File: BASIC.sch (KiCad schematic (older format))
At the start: 2 parts, among them U4 BASIC_ROM

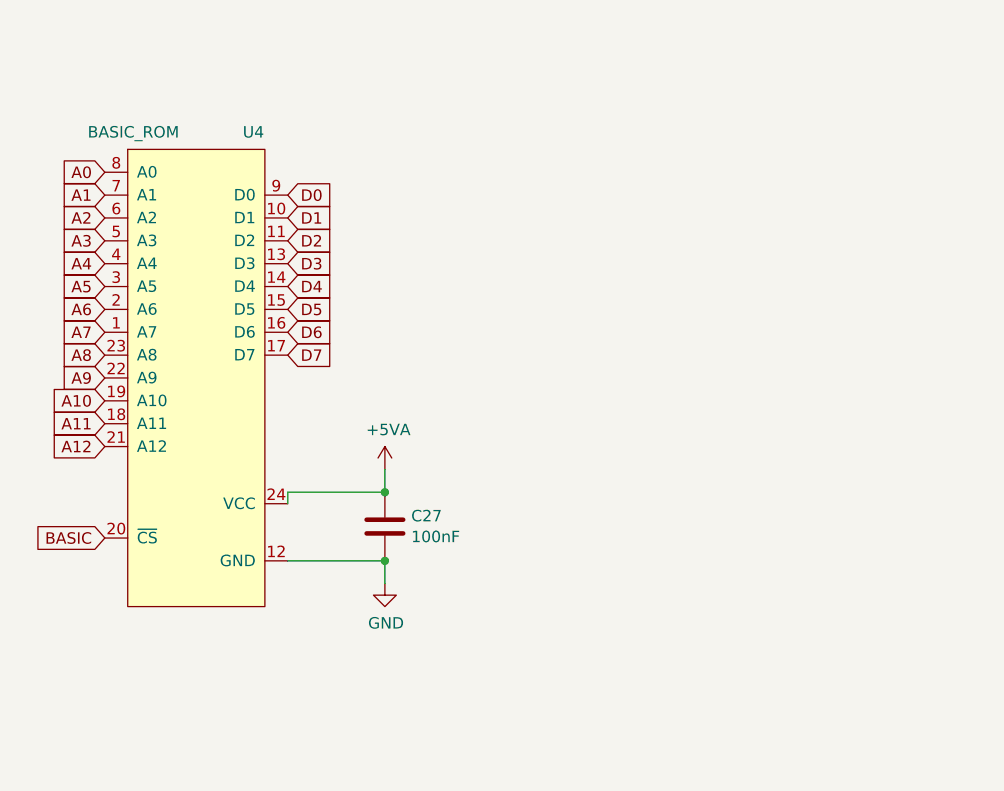
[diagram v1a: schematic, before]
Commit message: OSS and Basic in PLCC
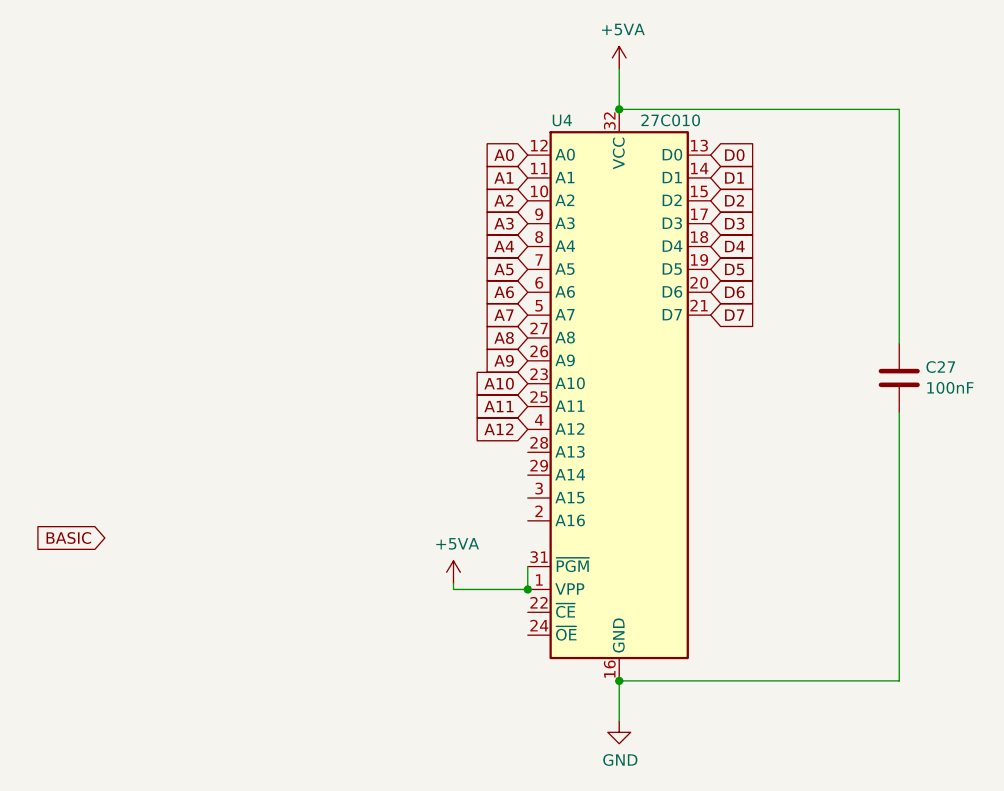
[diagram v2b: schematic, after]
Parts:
- removed U4: BASIC_ROM, Package_DIP:DIP-24_W15.24mm_Socket, symbol Atari:BASIC_ROM
- added U4: 27C010, Atari:PLCC-32_THT-Socket, symbol Memory_EPROM:27C010
- C27: footprint Atari:C_Axial_L5.1mm_D2.5mm_P12.50mm_Horizontal -> Capacitor_SMD:C_1206_3216Metric_Pad1.42x1.75mm_HandSolder
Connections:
- net +5VA: now also U4.1 (VPP), U4.31 (~PGM), U4.32 (VCC)
- net A0: now also U4.12 (A0)
- net A1: now also U4.11 (A1)
- net A10: now also U4.23 (A10)
- net A11: now also U4.25 (A11)
- net A12: now also U4.4 (A12)
- net A2: now also U4.10 (A2)
- net A3: now also U4.9 (A3)
- net A4: now also U4.8 (A4)
- net A5: now also U4.7 (A5)
- net A6: now also U4.6 (A6)
- net A7: now also U4.5 (A7)
- net A8: now also U4.27 (A8)
- net A9: now also U4.26 (A9)
- net D0: now also U4.13 (D0)
- net D1: now also U4.14 (D1)
- net D2: now also U4.15 (D2)
- net D3: now also U4.17 (D3)
- net D4: now also U4.18 (D4)
- net D5: now also U4.19 (D5)
- net D6: now also U4.20 (D6)
- net D7: now also U4.21 (D7)
- net GND: now also U4.16 (GND)
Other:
- moved on the sheet: C27
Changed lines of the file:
@@
 Comment4 ""
 $EndDescr
-Text GLabel 5675 2850 2    50   Input ~ 0
+Text GLabel 7525 2675 2    50   Input ~ 0
 D0
-Text GLabel 5675 2950 2    50   Input ~ 0
+Text GLabel 7525 2775 2    50   Input ~ 0
 D1
-Text GLabel 5675 3050 2    50   Input ~ 0
+Text GLabel 7525 2875 2    50   Input ~ 0
 D2
-Text GLabel 5675 3150 2    50   Input ~ 0
+Text GLabel 7525 2975 2    50   Input ~ 0
 D3
-Text GLabel 5675 3250 2    50   Input ~ 0
+Text GLabel 7525 3075 2    50   Input ~ 0
 D4
-Text GLabel 5675 3350 2    50   Input ~ 0
+Text GLabel 7525 3175 2    50   Input ~ 0
 D5
-Text GLabel 5675 3450 2    50   Input ~ 0
+Text GLabel 7525 3275 2    50   Input ~ 0
 D6
-Text GLabel 5675 3550 2    50   Input ~ 0
+Text GLabel 7525 3375 2    50   Input ~ 0
 D7
-Text GLabel 4875 2750 0    50   Input ~ 0
+Text GLabel 6725 2675 0    50   Input ~ 0
 A0
-Text GLabel 4875 2850 0    50   Input ~ 0
+Text GLabel 6725 2775 0    50   Input ~ 0
 A1
-Text GLabel 4875 2950 0    50   Input ~ 0
+Text GLabel 6725 2875 0    50   Input ~ 0
 A2
-Text GLabel 4875 3050 0    50   Input ~ 0
+Text GLabel 6725 2975 0    50   Input ~ 0
 A3
-Text GLabel 4875 3150 0    50   Input ~ 0
+Text GLabel 6725 3075 0    50   Input ~ 0
 A4
-Text GLabel 4875 3250 0    50   Input ~ 0
+Text GLabel 6725 3175 0    50   Input ~ 0
 A5
-Text GLabel 4875 3350 0    50   Input ~ 0
+Text GLabel 6725 3275 0    50   Input ~ 0
 A6
-Text GLabel 4875 3450 0    50   Input ~ 0
+Text GLabel 6725 3375 0    50   Input ~ 0
 A7
-Text GLabel 4875 3550 0    50   Input ~ 0
+Text GLabel 6725 3475 0    50   Input ~ 0
 A8
-Text GLabel 4875 3650 0    50   Input ~ 0
+Text GLabel 6725 3575 0    50   Input ~ 0
 A9
-Text GLabel 4875 3750 0    50   Input ~ 0
+Text GLabel 6725 3675 0    50   Input ~ 0
 A10
-Text GLabel 4875 3850 0    50   Input ~ 0
+Text GLabel 6725 3775 0    50   Input ~ 0
 A11
-Text GLabel 4875 3950 0    50   Input ~ 0
+Text GLabel 6725 3875 0    50   Input ~ 0
 A12
 Text GLabel 4875 4350 0    50   Input ~ 0
@@
 L Device:C C27
 U 1 1 6020CFCE
-P 6100 4300
-F 0 "C27" H 6215 4346 50  0000 L CNN
-F 1 "100nF" H 6215 4255 50  0000 L CNN
-F 2 "Atari:C_Axial_L5.1mm_D2.5mm_P12.50mm_Horizontal" H 6138 4150 50  0001 C CNN
-F 3 "~" H 6100 4300 50  0001 C CNN
-	1    6100 4300
+P 8350 3650
+F 0 "C27" H 8465 3696 50  0000 L CNN
+F 1 "100nF" H 8465 3605 50  0000 L CNN
+F 2 "Capacitor_SMD:C_1206_3216Metric_Pad1.42x1.75mm_HandSolder" H 8388 3500 50  0001 C CNN
+F 3 "~" H 8350 3650 50  0001 C CNN
+	1    8350 3650
 	1    0    0    -1
 $EndComp
@@
 L power:+5VA #PWR0145
 U 1 1 6020DDBE
-P 6100 4050
-F 0 "#PWR0145" H 6100 3900 50  0001 C CNN
-F 1 "+5VA" H 6115 4223 50  0000 C CNN
-F 2 "" H 6100 4050 50  0001 C CNN
-F 3 "" H 6100 4050 50  0001 C CNN
-	1    6100 4050
+P 7125 2300
+F 0 "#PWR0145" H 7125 2150 50  0001 C CNN
+F 1 "+5VA" H 7140 2473 50  0000 C CNN
+F 2 "" H 7125 2300 50  0001 C CNN
+F 3 "" H 7125 2300 50  0001 C CNN
+	1    7125 2300
 	1    0    0    -1
 $EndComp
@@
 L power:GND #PWR0146
 U 1 1 6020E6E5
-P 6100 4550
-F 0 "#PWR0146" H 6100 4300 50  0001 C CNN
-F 1 "GND" H 6105 4377 50  0000 C CNN
-F 2 "" H 6100 4550 50  0001 C CNN
-F 3 "" H 6100 4550 50  0001 C CNN
-	1    6100 4550
+P 7125 5150
+F 0 "#PWR0146" H 7125 4900 50  0001 C CNN
+F 1 "GND" H 7130 4977 50  0000 C CNN
+F 2 "" H 7125 5150 50  0001 C CNN
+F 3 "" H 7125 5150 50  0001 C CNN
+	1    7125 5150
 	1    0    0    -1
 $EndComp
 $Comp
-L Atari:BASIC_ROM U4
-U 1 1 60211097
-P 5275 3650
-F 0 "U4" H 5525 4725 50  0000 C CNN
-F 1 "BASIC_ROM" H 5000 4725 50  0000 C CNN
-F 2 "Package_DIP:DIP-24_W15.24mm_Socket" H 5275 3650 50  0001 C CNN
-F 3 "" H 5275 3650 50  0001 C CNN
-	1    5275 3650
+L Memory_EPROM:27C010 U4
+U 1 1 60AA9A56
+P 7125 3675
+F 0 "U4" H 6875 4825 50  0000 C CNN
+F 1 "27C010" H 7350 4825 50  0000 C CNN
+F 2 "Atari:PLCC-32_THT-Socket" H 7125 3675 50  0001 C CNN
+F 3 "http://ww1.microchip.com/downloads/en/DeviceDoc/doc0321.pdf" H 7125 3675 50  0001 C CNN
+	1    7125 3675
 	1    0    0    -1
 $EndComp
 Wire Wire Line
-	5675 4450 6100 4450
+	7125 2475 8350 2475
 Wire Wire Line
-	6100 4150 5675 4150
+	8350 2475 8350 3500
 Wire Wire Line
-	5675 4150 5675 4200
+	7125 4975 8350 4975
 Wire Wire Line
-	6100 4050 6100 4150
-Connection ~ 6100 4150
+	8350 4975 8350 3800
 Wire Wire Line
-	6100 4550 6100 4450
-Connection ~ 6100 4450
+	7125 2300 7125 2475
+Connection ~ 7125 2475
+Wire Wire Line
+	7125 5150 7125 4975
+Connection ~ 7125 4975
+Wire Wire Line
+	6725 4475 6725 4575
+$Comp
+L power:+5VA #PWR0254
+U 1 1 60AACE4B
+P 6400 4550
+F 0 "#PWR0254" H 6400 4400 50  0001 C CNN
+F 1 "+5VA" H 6415 4723 50  0000 C CNN
+F 2 "" H 6400 4550 50  0001 C CNN
+F 3 "" H 6400 4550 50  0001 C CNN
+	1    6400 4550
+	1    0    0    -1
+$EndComp
+Wire Wire Line
+	6725 4575 6400 4575
+Wire Wire Line
+	6400 4575 6400 4550
+Connection ~ 6725 4575
 $EndSCHEMATC

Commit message: SuperCart
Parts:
- added C207: 100nF, Capacitor_SMD:C_1206_3216Metric_Pad1.42x1.75mm_HandSolder, symbol Device:C
- added J211: Conn_01x02, Connector_PinHeader_2.54mm:PinHeader_1x02_P2.54mm_Vertical, symbol Connector_Generic:Conn_01x02
- added R502: 1k, Resistor_SMD:R_1206_3216Metric_Pad1.42x1.75mm_HandSolder, symbol Device:R
- added R503: 10k, Resistor_SMD:R_1206_3216Metric_Pad1.42x1.75mm_HandSolder, symbol Device:R
- added U100: 74LS157, Package_SO:SOIC-16_3.9x9.9mm_P1.27mm, symbol 74xx:74LS157
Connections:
- net +5VA: now also C207.1, R503.1, U100.16 (VCC), U100.6 (I1b)
- net A12: now also U100.3 (I1a); no longer U4.4 (A12)
- net BASIC: now also U100.10 (I1c)
- net GND: now also C207.2, J211.2 (Pin_2), R502.2, U100.15 (E), U100.8 (GND)
- net A16_sel: now reaches U4.2 (A16)
- net at U4.22 (~CE): now also U4.24 (~OE), U100.9 (Zc)
- net at U4.28 (A13): now also U100.7 (Zb)
- net A14_sel: now reaches U4.29 (A14)
- net A15_sel: now reaches U4.3 (A15)
- new net: U100.4 (Za), U4.4 (A12)
- new net: J211.1 (Pin_1), R503.2, U100.1 (S)
- new net: R502.1, U100.13 (I1d)
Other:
- moved on the sheet: C27, U4

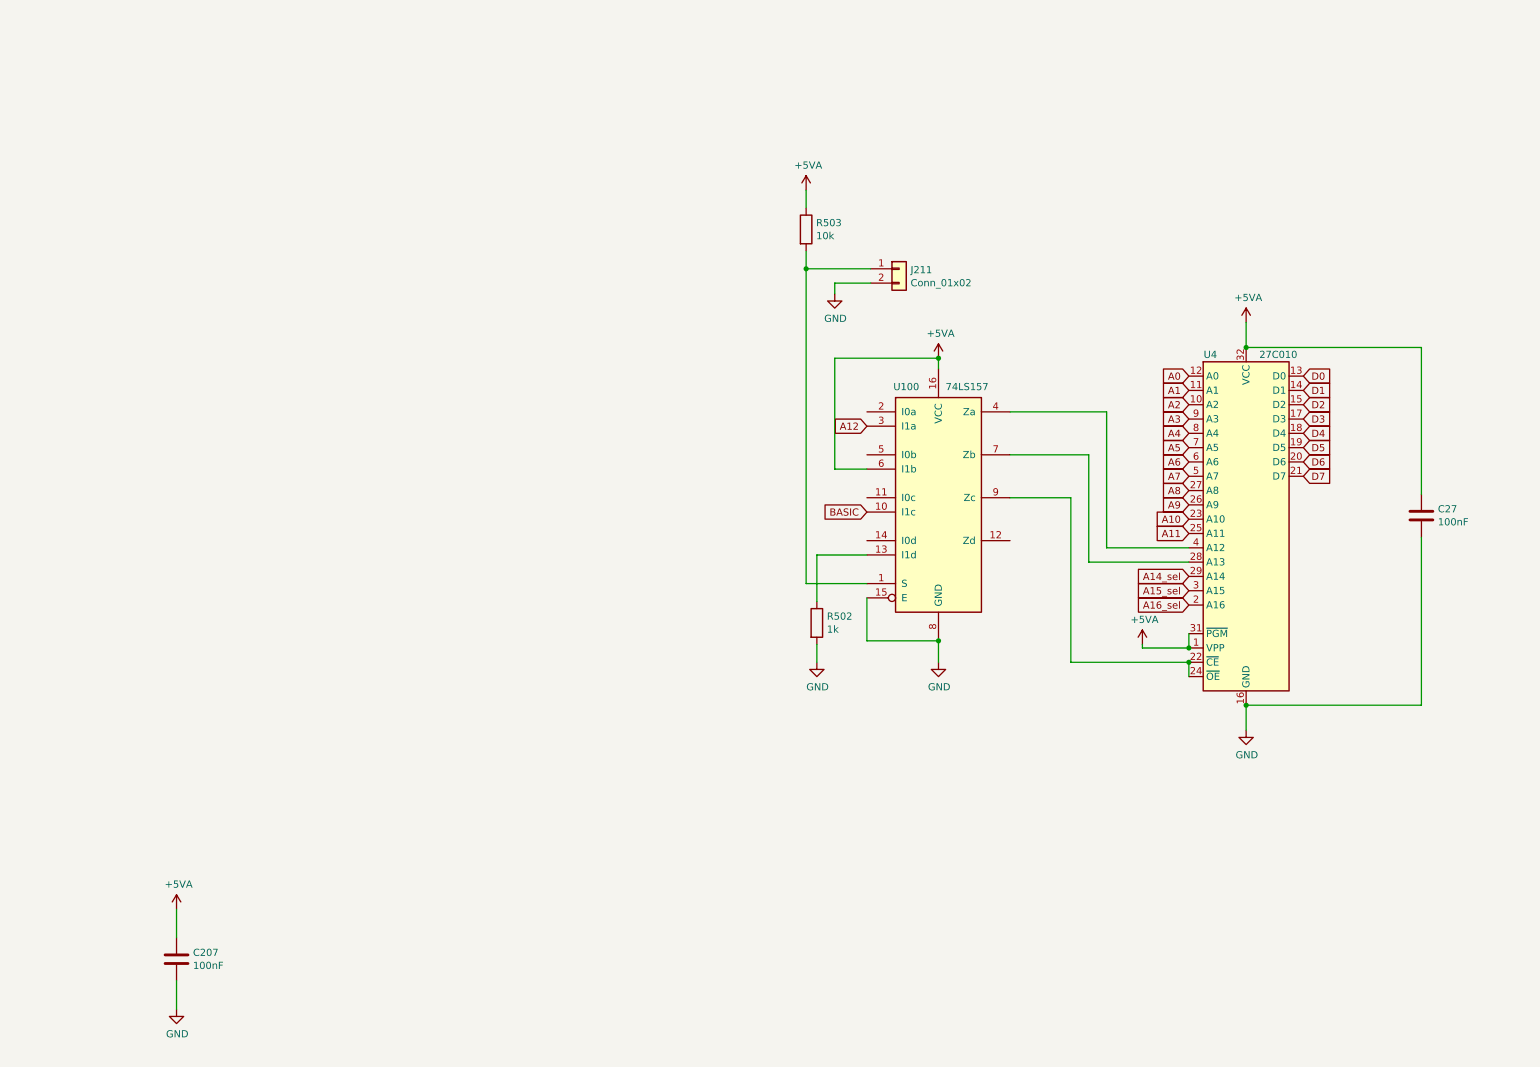
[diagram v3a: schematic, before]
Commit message: Add Basci and SO PLCC
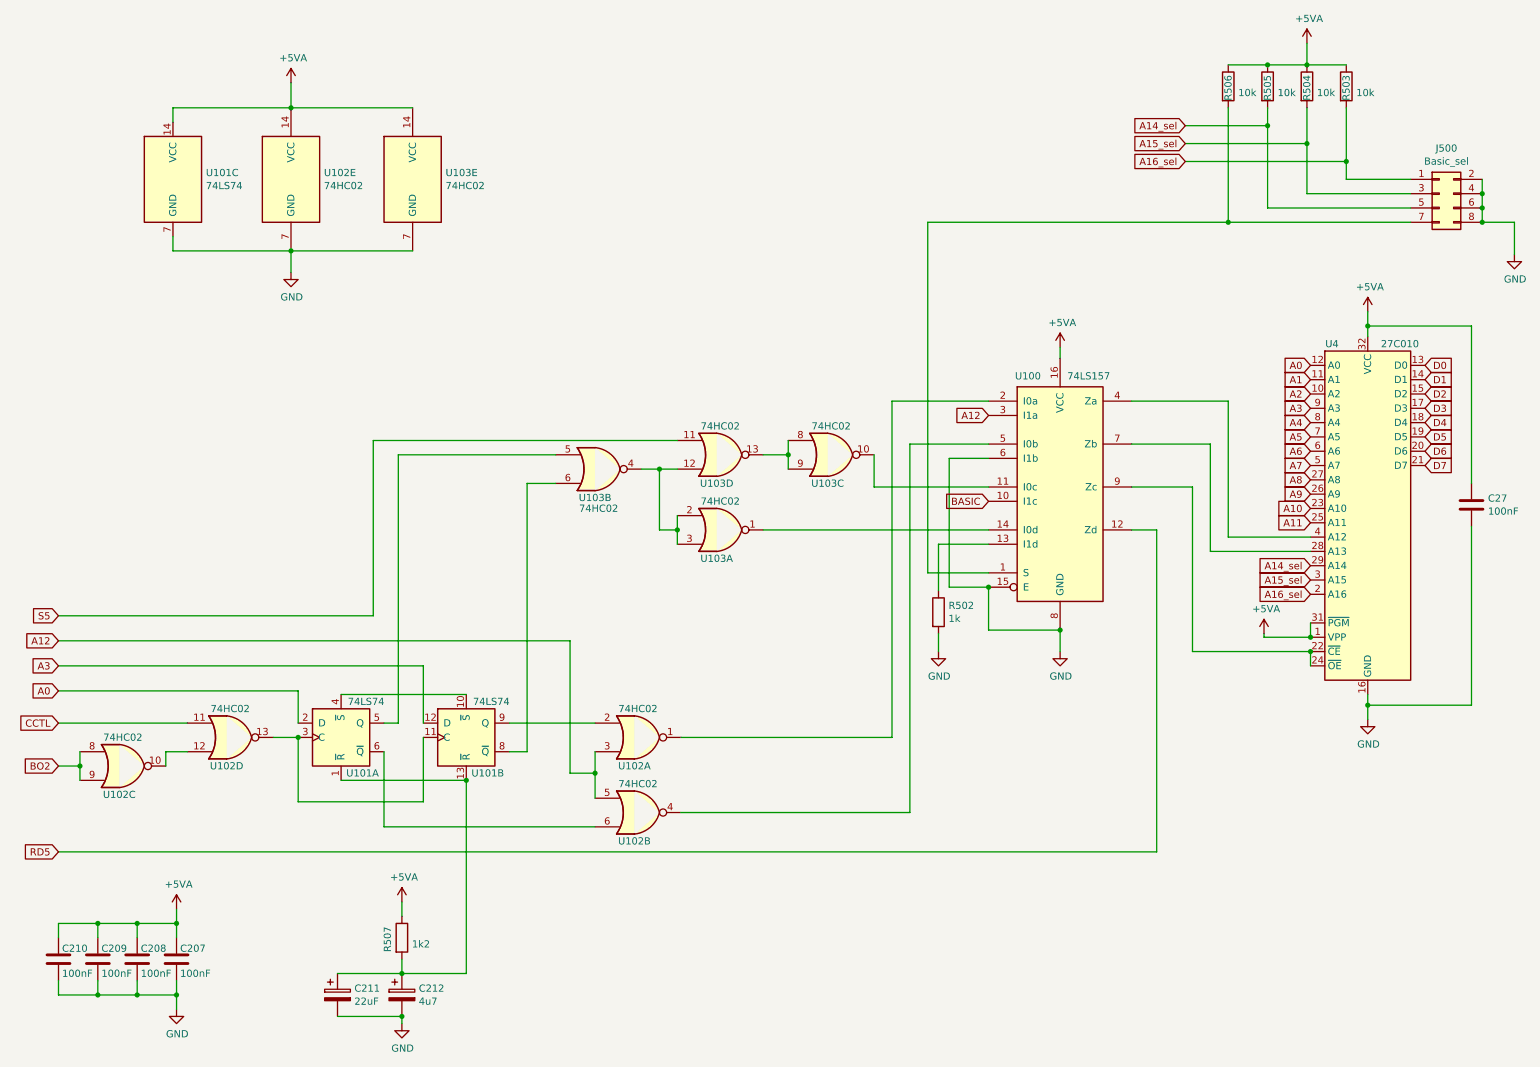
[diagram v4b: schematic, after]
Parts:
- removed J211: Conn_01x02, Connector_PinHeader_2.54mm:PinHeader_1x02_P2.54mm_Vertical, symbol Connector_Generic:Conn_01x02
- added C208, C209, C210: 100nF, Capacitor_SMD:C_1206_3216Metric_Pad1.42x1.75mm_HandSolder, symbol Device:C
- added C211: 22uF, Capacitor_Tantalum_SMD:CP_EIA-3528-21_Kemet-B_Pad1.50x2.35mm_HandSolder, symbol Device:CP
- added C212: 4u7, Capacitor_Tantalum_SMD:CP_EIA-3528-21_Kemet-B_Pad1.50x2.35mm_HandSolder, symbol Device:CP
- added J500: Basic_sel, Connector_PinHeader_2.54mm:PinHeader_2x04_P2.54mm_Vertical, symbol Connector_Generic:Conn_02x04_Odd_Even
- added R503, R504, R505: 10k, Resistor_SMD:R_1206_3216Metric_Pad1.42x1.75mm_HandSolder, symbol Device:R
- added R507: 1k2, Resistor_SMD:R_1206_3216Metric_Pad1.42x1.75mm_HandSolder, symbol Device:R
- added U101: 74LS74, Package_SO:SOIC-14_3.9x8.7mm_P1.27mm, symbol 74xx:74LS74
- added U102, U103: 74HC02, Package_SO:SOIC-14_3.9x8.7mm_P1.27mm, symbol 74xx:74HC02
- renumbered R503 to R506
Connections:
- net +5VA: now also C208.1, C209.1, C210.1, R503.1, R504.1, R505.1, R507.1, U101.14 (VCC), U102.14 (VCC), U103.14 (VCC); no longer U100.6 (I1b)
- net A0: now also U101.2 (D)
- net A12: now also U102.3, U102.5
- net A14_sel: now also J500.5 (Pin_5), R505.2
- net A15_sel: now also J500.3 (Pin_3), R504.2
- net A16_sel: now also J500.1 (Pin_1), R503.2
- net A3: now also U101.12 (D)
- net GND: now also U100.6 (I1b), C208.2, C209.2, C210.2, C211.2, C212.2, J500.2 (Pin_2), J500.4 (Pin_4), J500.6 (Pin_6), J500.8 (Pin_8), U101.7 (GND), U102.7 (GND), U103.7 (GND)
- net at R506.2, U100.1 (S): now also J500.7 (Pin_7)
- net at U100.11 (I0c): now also U103.10
- net RD5: now reaches U100.12 (Zd)
- net at U100.14 (I0d): now also U103.1
- net at U100.2 (I0a): now also U102.1
- net at U100.5 (I0b): now also U102.4
- new net: C211.1, C212.1, R507.2, U101.1 (~R), U101.13 (~R)
- new net: U101.11 (C), U101.3 (C), U102.13
- new net: U101.10 (~S), U101.4 (~S)
- new net: U101.5 (Q), U103.5
- new net: U101.6 (~Q), U102.6
- new net: U101.8 (~Q), U103.6
- new net: U101.9 (Q), U102.2
- new net: U102.10, U102.12
- new net: U103.12, U103.2, U103.3, U103.4
- new net: U103.13, U103.8, U103.9
- new net BO2: U102.8, U102.9
- new net CCTL: U102.11
- new net S5: U103.11
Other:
- moved on the sheet: C27, R502, R506, U100, U4
